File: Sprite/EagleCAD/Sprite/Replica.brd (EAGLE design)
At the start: 35 x 35 mm, 25 parts, among them U1 CC430F5137, X1 26 MHz

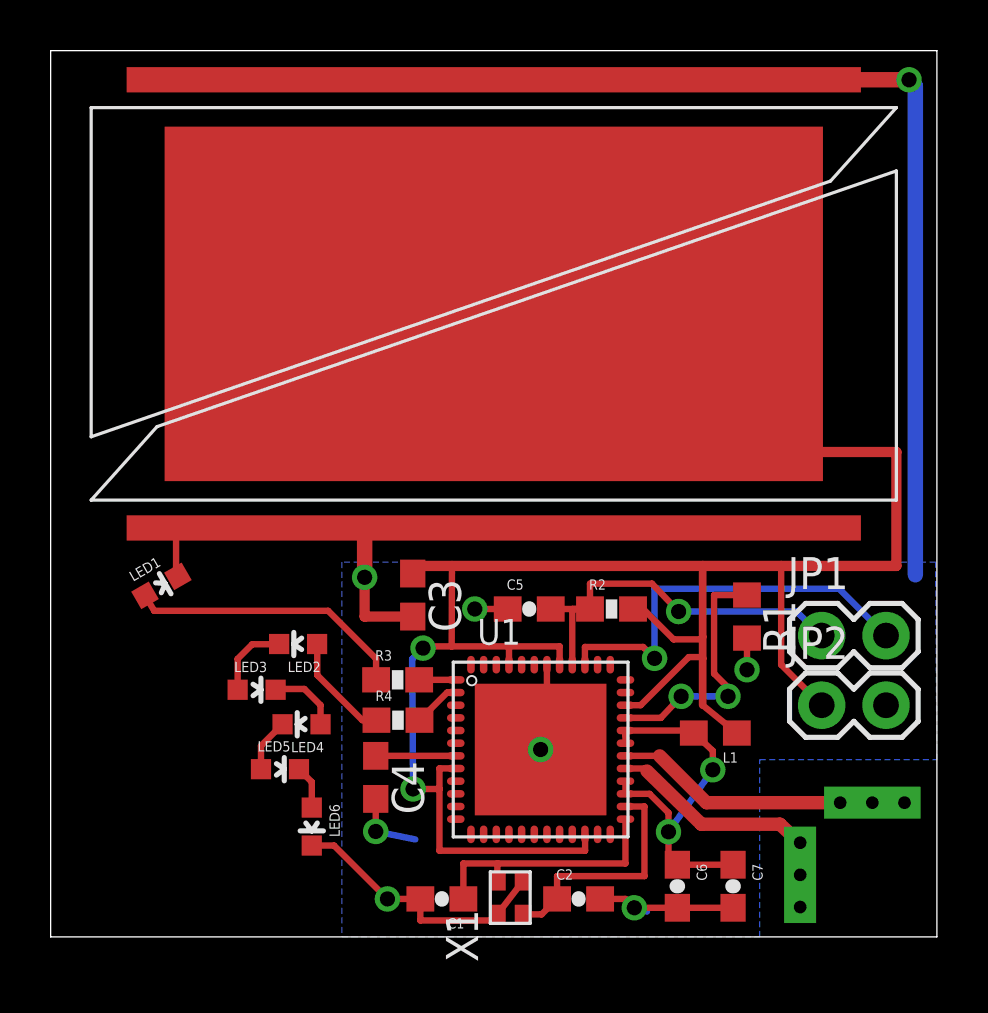
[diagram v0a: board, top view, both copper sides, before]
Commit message: Replica board - put each LED on it's own pin
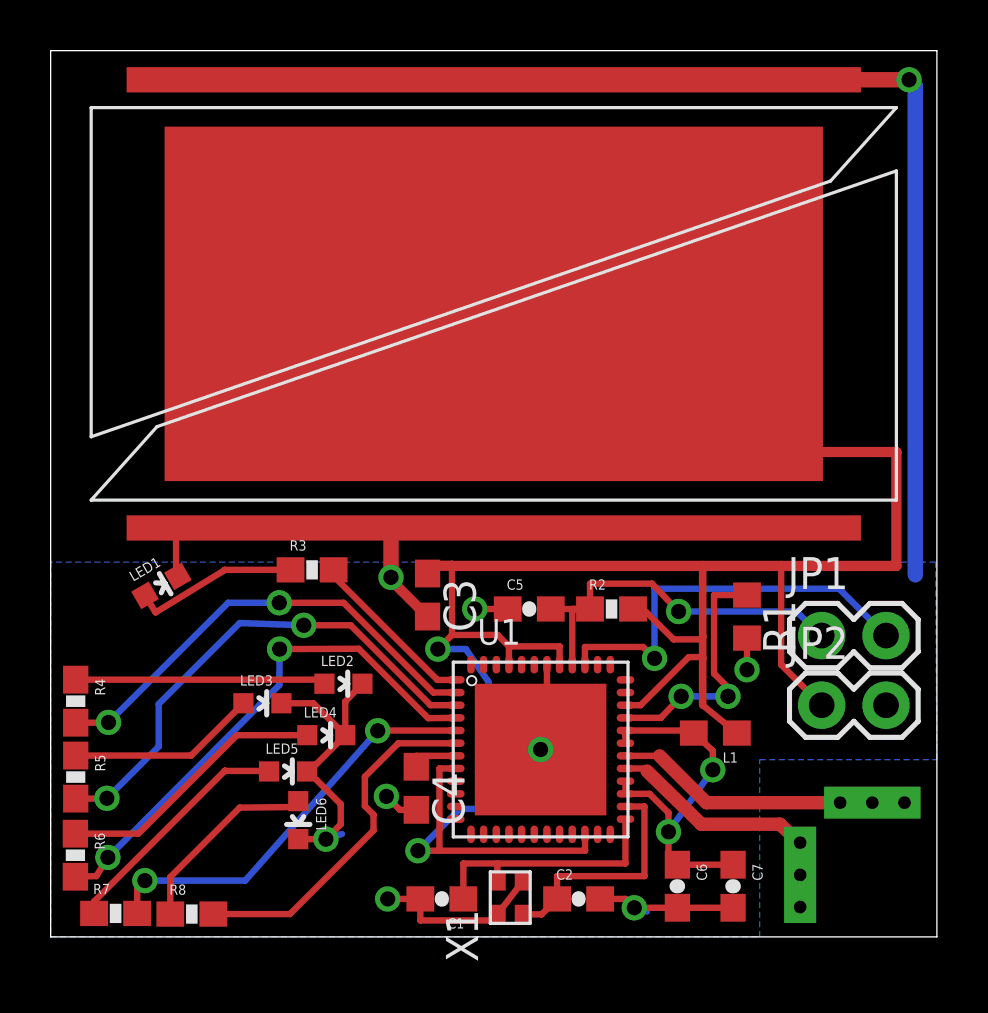
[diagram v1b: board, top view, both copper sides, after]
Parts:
- added R5, R6, R7, R8: 270R, SparkFun:0603-RES
- moved R4 12.7 mm to (0.99, 9.31), turned to 270 degrees
- moved R3 5.50 mm to (10.3, 14.5)
- moved LED2 2.38 mm to (11.6, 10.00), turned to 270 degrees
- moved C4 1.66 mm to (14.4, 5.87)
- moved LED4 1.07 mm to (10.9, 7.97), turned to 270 degrees
- moved LED6 0.59 mm to (9.78, 4.61)
- moved C3 0.58 mm to (14.9, 13.5)
- moved LED3 0.58 mm to (8.36, 9.23)
- moved LED5 0.33 mm to (9.37, 6.53)
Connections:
- net N$4 renamed VCORE
- new net N$13: R5.2, U1.3
- new net N$14: R6.2, U1.4
- new net N$15: R7.2, U1.5
- new net N$16: R8.2, U1.6
- net GND: now also LED2.C, LED3.C, LED4.C, LED5.C
- net N$10: now also R8.1; no longer LED5.C
- net N$7: now also R5.1; no longer LED2.C
- net N$8: now also R6.1; no longer LED3.C
- net N$9: now also R7.1; no longer LED4.C
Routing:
- net N$14: track 0.00 -> 20.8 mm, vias 0 -> 2
- net N$13: track 0.00 -> 20.2 mm, vias 0 -> 2
- net N$5: track 1.89 -> 18.4 mm, vias 0 -> 2
- net N$15: track 0.00 -> 16.4 mm, vias 0 -> 2
- net N$16: track 0.00 -> 14.1 mm
- net GND: track 82.9 -> 91.6 mm, vias 8 -> 9
- net N$8: track 2.81 -> 10.8 mm
- net N$9: track 2.13 -> 9.53 mm
- net N$10: track 1.73 -> 7.87 mm
- net N$6: track 4.31 -> 9.89 mm
- net N$11: track 1.45 -> 6.83 mm
- net N$12: track 11.1 -> 6.62 mm
- net N$7: track 3.10 -> 7.48 mm
- net VCC: track 93.3 -> 97.3 mm
- net VCORE: track 3.16 -> 1.99 mm

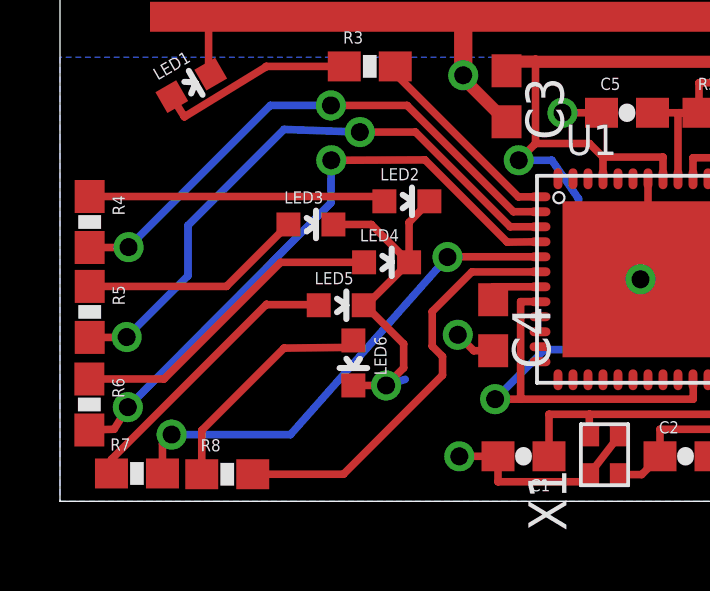
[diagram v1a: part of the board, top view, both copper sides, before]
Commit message: Tweaked replica board for Sunstone design rules
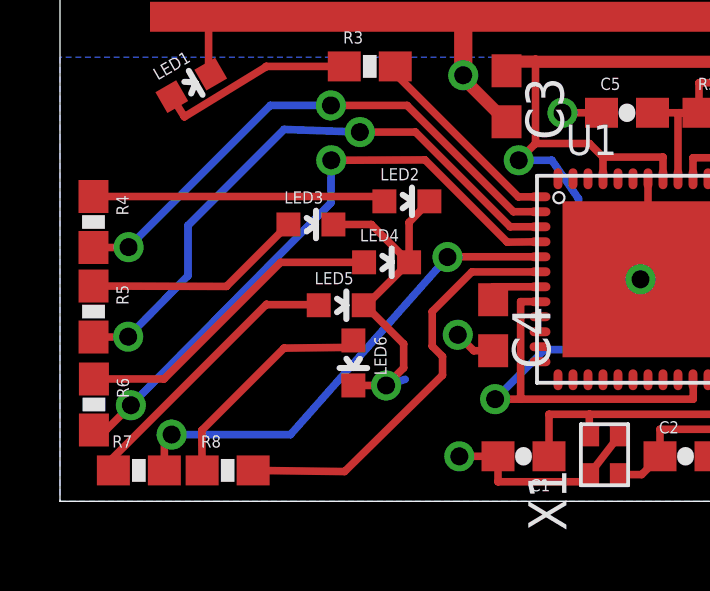
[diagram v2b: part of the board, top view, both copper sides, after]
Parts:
- moved R6 0.15 mm to (1.13, 3.23)
- moved R8 0.13 mm to (5.59, 1.03)
- moved R5 0.13 mm to (1.12, 6.32)
- moved R4 0.13 mm to (1.12, 9.31)
- moved R7 0.12 mm to (2.63, 1.03)
